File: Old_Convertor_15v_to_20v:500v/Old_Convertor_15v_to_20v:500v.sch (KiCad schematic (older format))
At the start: 54 parts, among them J1 Screw_Terminal_01x04, J2 Conn_01x04_Male, Q1 IRF640NSTR, T1 Transfomer_1P_1S_custom, U1 OP177, U10 PVN012, U2 UC3845, U3 DCP011515D, U4 ISO124P, U5 DCP011515D, U6 CPC1977, U7 CPC1977, U8 CPC1977, U9 CPC1977

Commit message: old_convertor done
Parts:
- R10: value 36k 1% -> 30k 1%
- R7: value 0.2 0.25W -> 0.2
- U2: value UC3845 -> UC3845_DIP8
- renumbered C7 to C10, C12 to C11, C14 to C12, C12 to C13, C13 to C14, C6 to C5, C5 to C6, C8 to C7, C9 to C8, C10 to C9, R16 to R15, R15 to R16, R17 to R18, U9 to U10, U10 to U8, U8 to U9
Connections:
- net +15V: now also C12.1; no longer C13.1
- net GND: now also C12.2; no longer C13.2
- net GND2: now also C13.2; no longer C12.2
- net at U4.1 (+Vs1), U5.6 (+Vout): now also C13.1; no longer C12.1
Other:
- moved on the sheet: C12, C13, C14, R15, U8

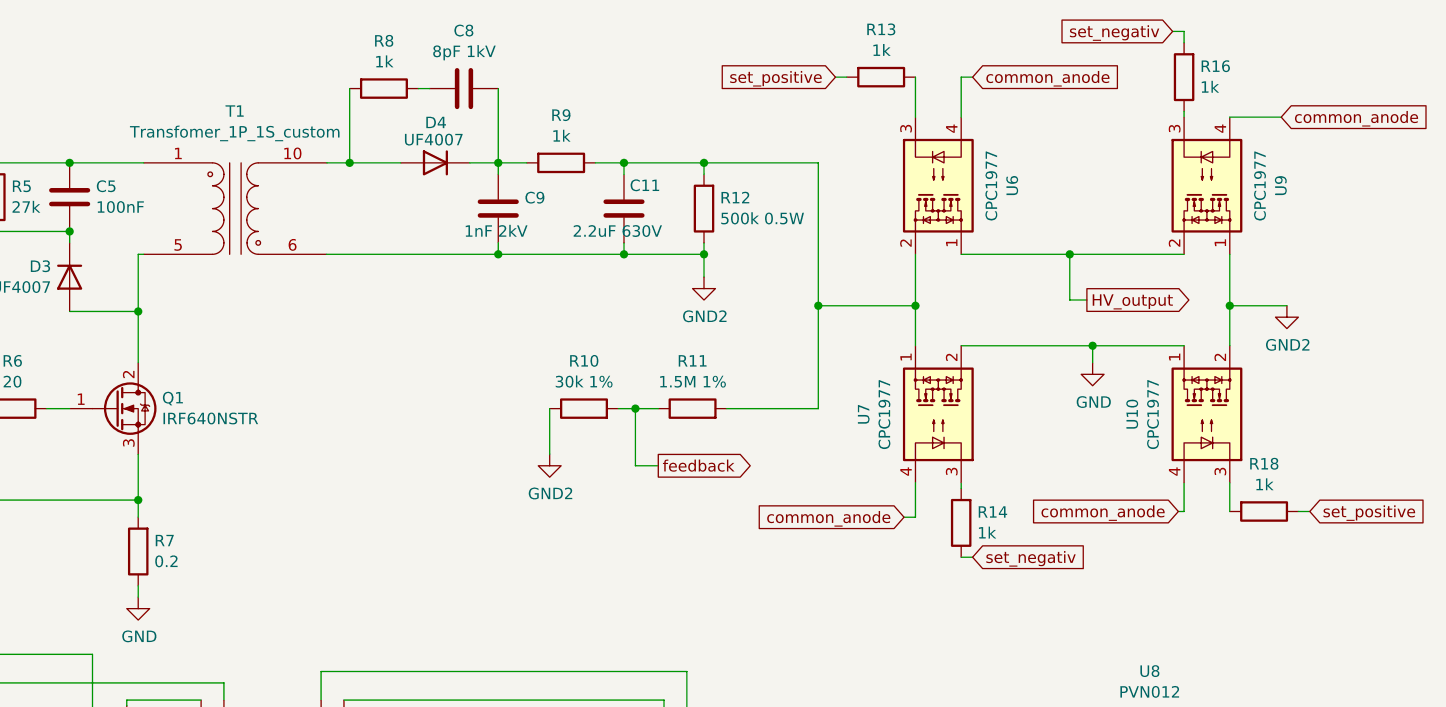
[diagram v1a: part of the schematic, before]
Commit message: edit resitors cpc1977
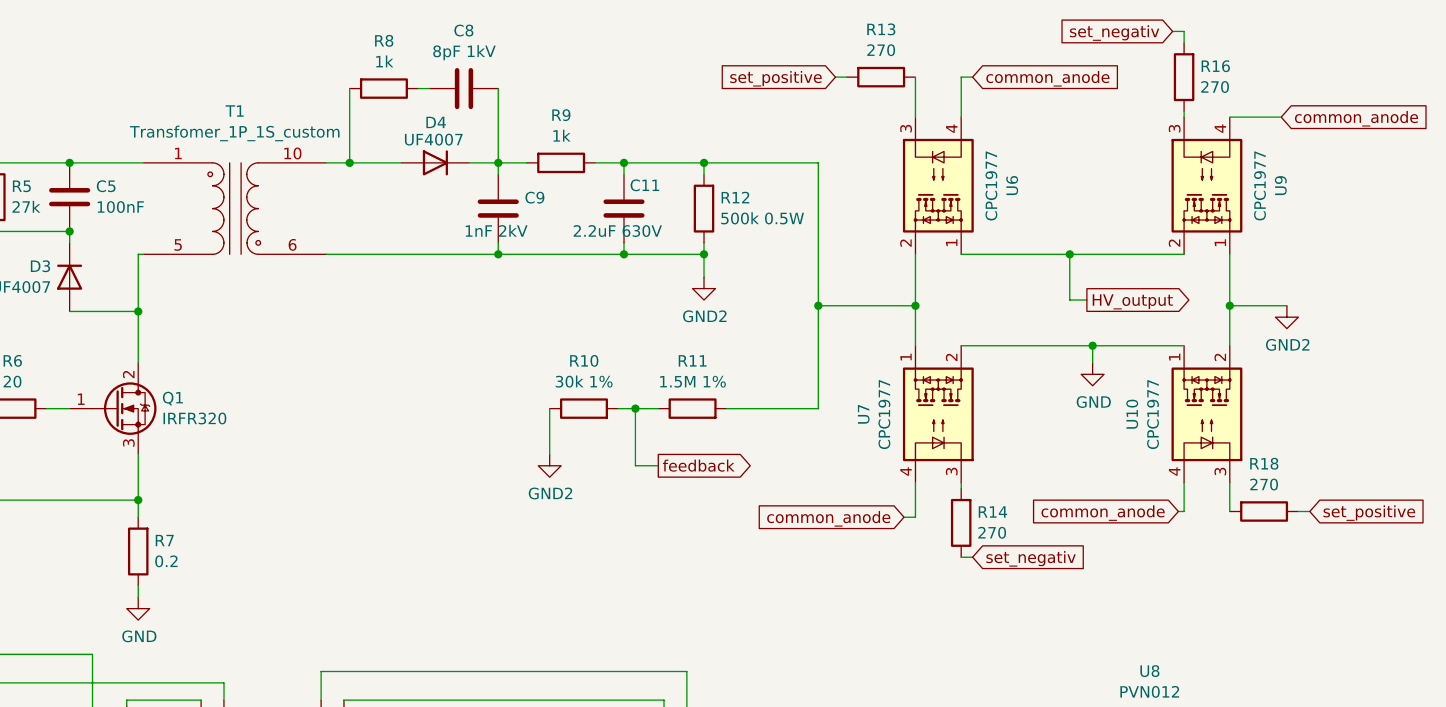
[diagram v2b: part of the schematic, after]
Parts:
- Q1: value IRF640NSTR -> IRFR320
- R13, R14, R16, R18: value 1k -> 270
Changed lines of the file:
@@
 P 4600 2700
 F 0 "Q1" H 4804 2746 50  0000 L CNN
-F 1 "IRF640NSTR" H 4804 2655 50  0000 L CNN
+F 1 "IRFR320" H 4804 2655 50  0000 L CNN
 F 2 "Package_TO_SOT_SMD:TO-252-2" H 4850 2625 50  0001 L CIN
 F 3 "http://www.irf.com/product-info/datasheets/data/irf540n.pdf" H 4600 2700 50  0001 L CNN
@@
 P 8300 3200
 F 0 "R14" H 8230 3154 50  0000 R CNN
-F 1 "1k" H 8230 3245 50  0000 R CNN
+F 1 "270" H 8230 3245 50  0000 R CNN
 F 2 "Resistor_SMD:R_0805_2012Metric" V 8230 3200 50  0001 C CNN
 F 3 "~" H 8300 3200 50  0001 C CNN
@@
 P 9275 1250
 F 0 "R16" H 9205 1204 50  0000 R CNN
-F 1 "1k" H 9205 1295 50  0000 R CNN
+F 1 "270" H 9205 1295 50  0000 R CNN
 F 2 "Resistor_SMD:R_0805_2012Metric" V 9205 1250 50  0001 C CNN
 F 3 "~" H 9275 1250 50  0001 C CNN
@@
 P 7950 1250
 F 0 "R13" V 7743 1250 50  0000 C CNN
-F 1 "1k" V 7834 1250 50  0000 C CNN
+F 1 "270" V 7834 1250 50  0000 C CNN
 F 2 "Resistor_SMD:R_0805_2012Metric" V 7880 1250 50  0001 C CNN
 F 3 "~" H 7950 1250 50  0001 C CNN
@@
 P 9625 3150
 F 0 "R18" V 9418 3150 50  0000 C CNN
-F 1 "1k" V 9509 3150 50  0000 C CNN
+F 1 "270" V 9509 3150 50  0000 C CNN
 F 2 "Resistor_SMD:R_0805_2012Metric" V 9555 3150 50  0001 C CNN
 F 3 "~" H 9625 3150 50  0001 C CNN
